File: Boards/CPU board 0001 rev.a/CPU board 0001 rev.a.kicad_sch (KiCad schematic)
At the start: 78 parts, among them J1 CEC card edge connector large, U10 7432, U11 7442, U12 7406, U13 7406, U14 7442, U15 7442, U16 M8216, U17 M8216, U18 6532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

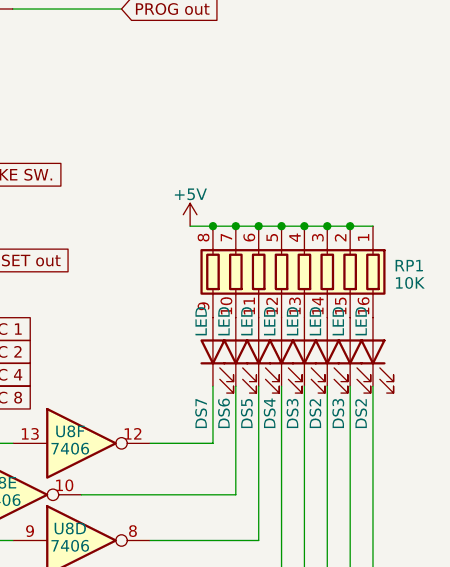
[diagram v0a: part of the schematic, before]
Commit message: revisions from real life boards
tip130a is actually tip30a, widened holes for crystal, widened holes for big power resistor, fixed cpu board LED resistors
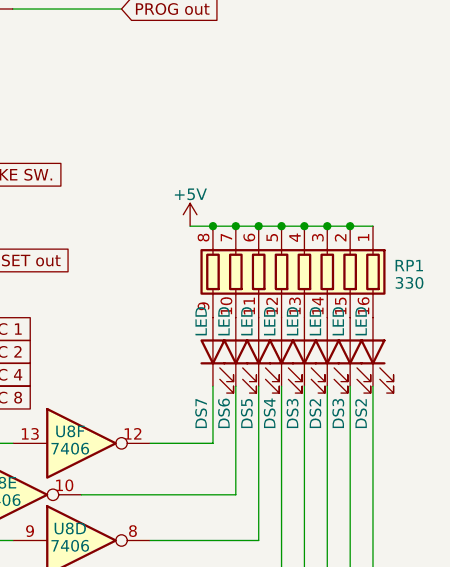
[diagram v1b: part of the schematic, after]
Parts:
- RP1: value 10K -> 330
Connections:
- net at U18.18 (PB5): now also U12.3
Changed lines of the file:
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@@
       (effects (font (size 1.27 1.27)) (justify left))
     )
-    (property "Value" "10K" (at 485.14 139.7 0)
+    (property "Value" "330" (at 485.14 139.7 0)
       (effects (font (size 1.27 1.27)) (justify left))
     )
